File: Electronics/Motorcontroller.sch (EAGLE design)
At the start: 33 parts, among them Q1 IRFZ48V, Q2 IRF4905V, Q3 IRFZ48V, Q4 IRF4905V, Q5 IRFZ48V, Q6 IRF4905V, Q7 IRFZ48V, Q8 IRF4905V, X3 24V Batt

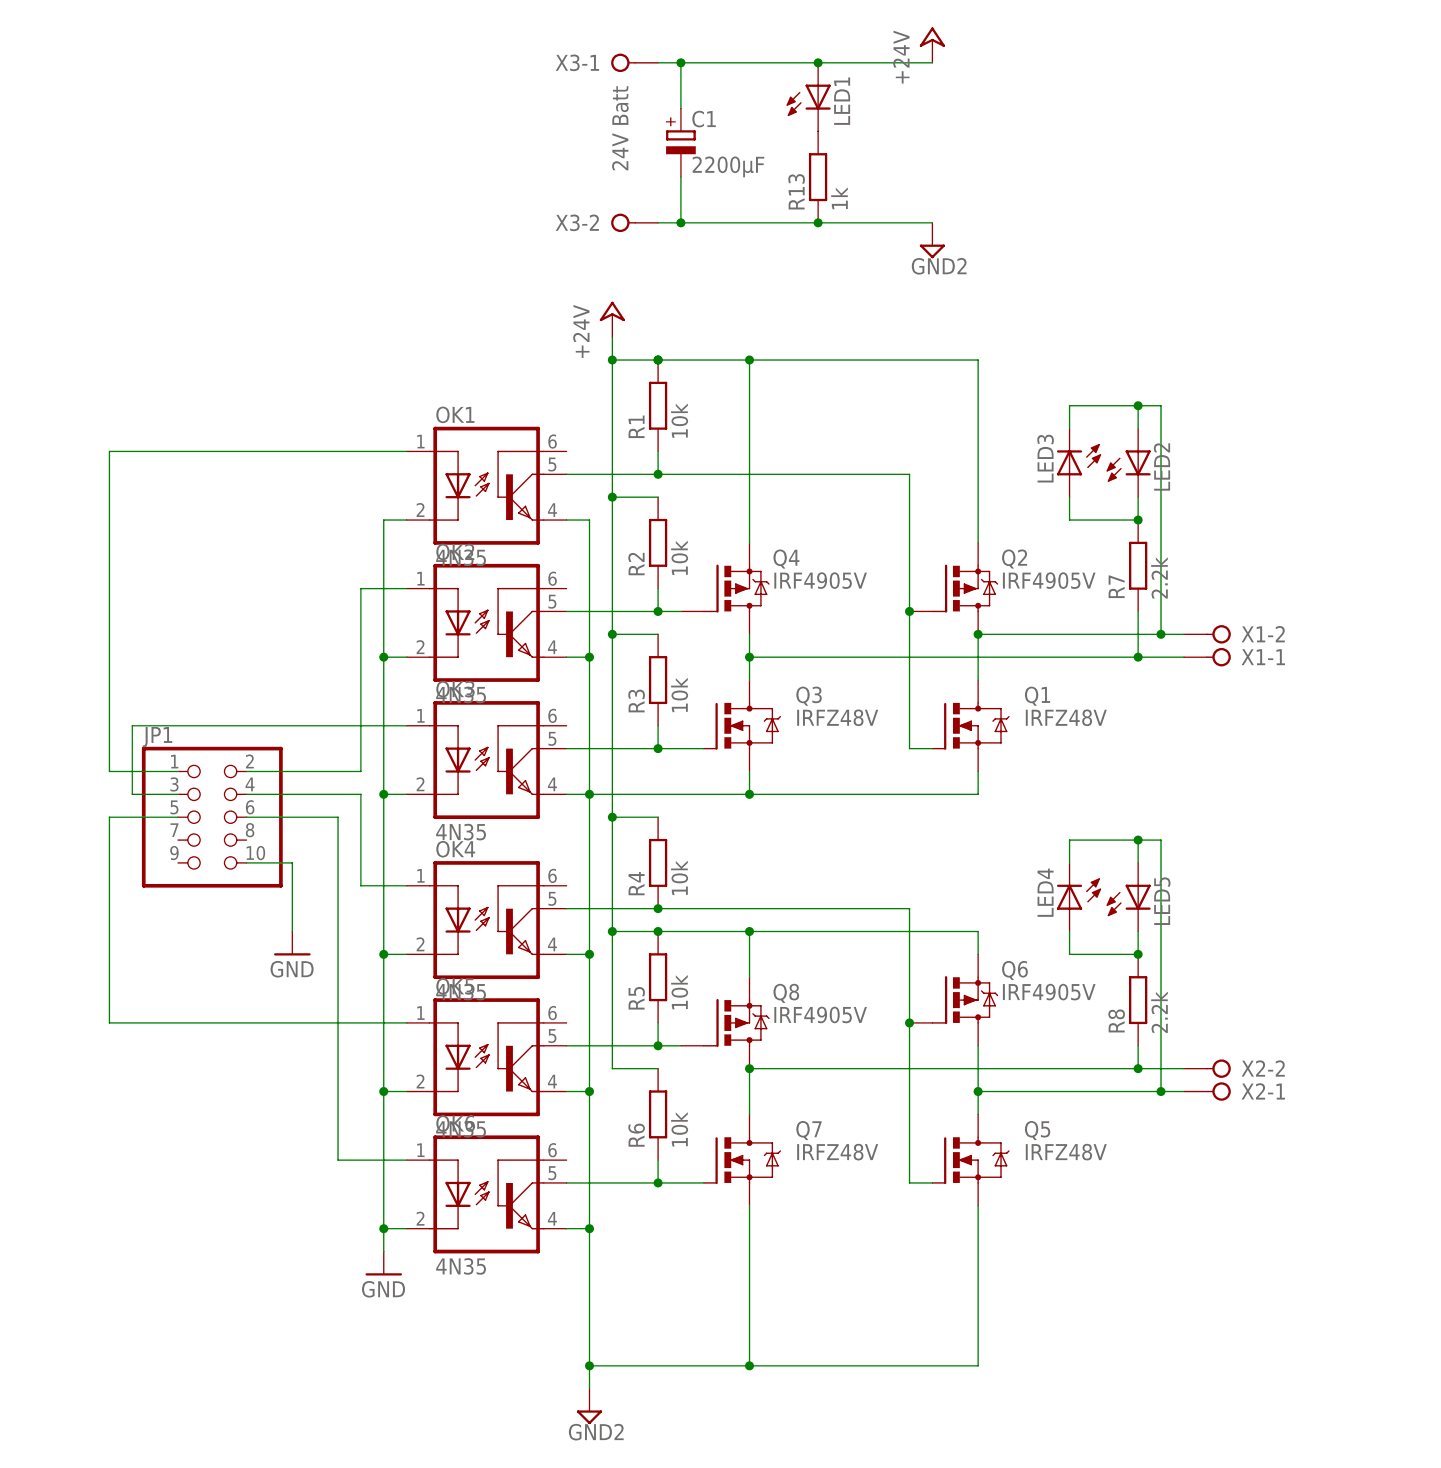
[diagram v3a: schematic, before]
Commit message: Redesign of motorboard. Closes #30
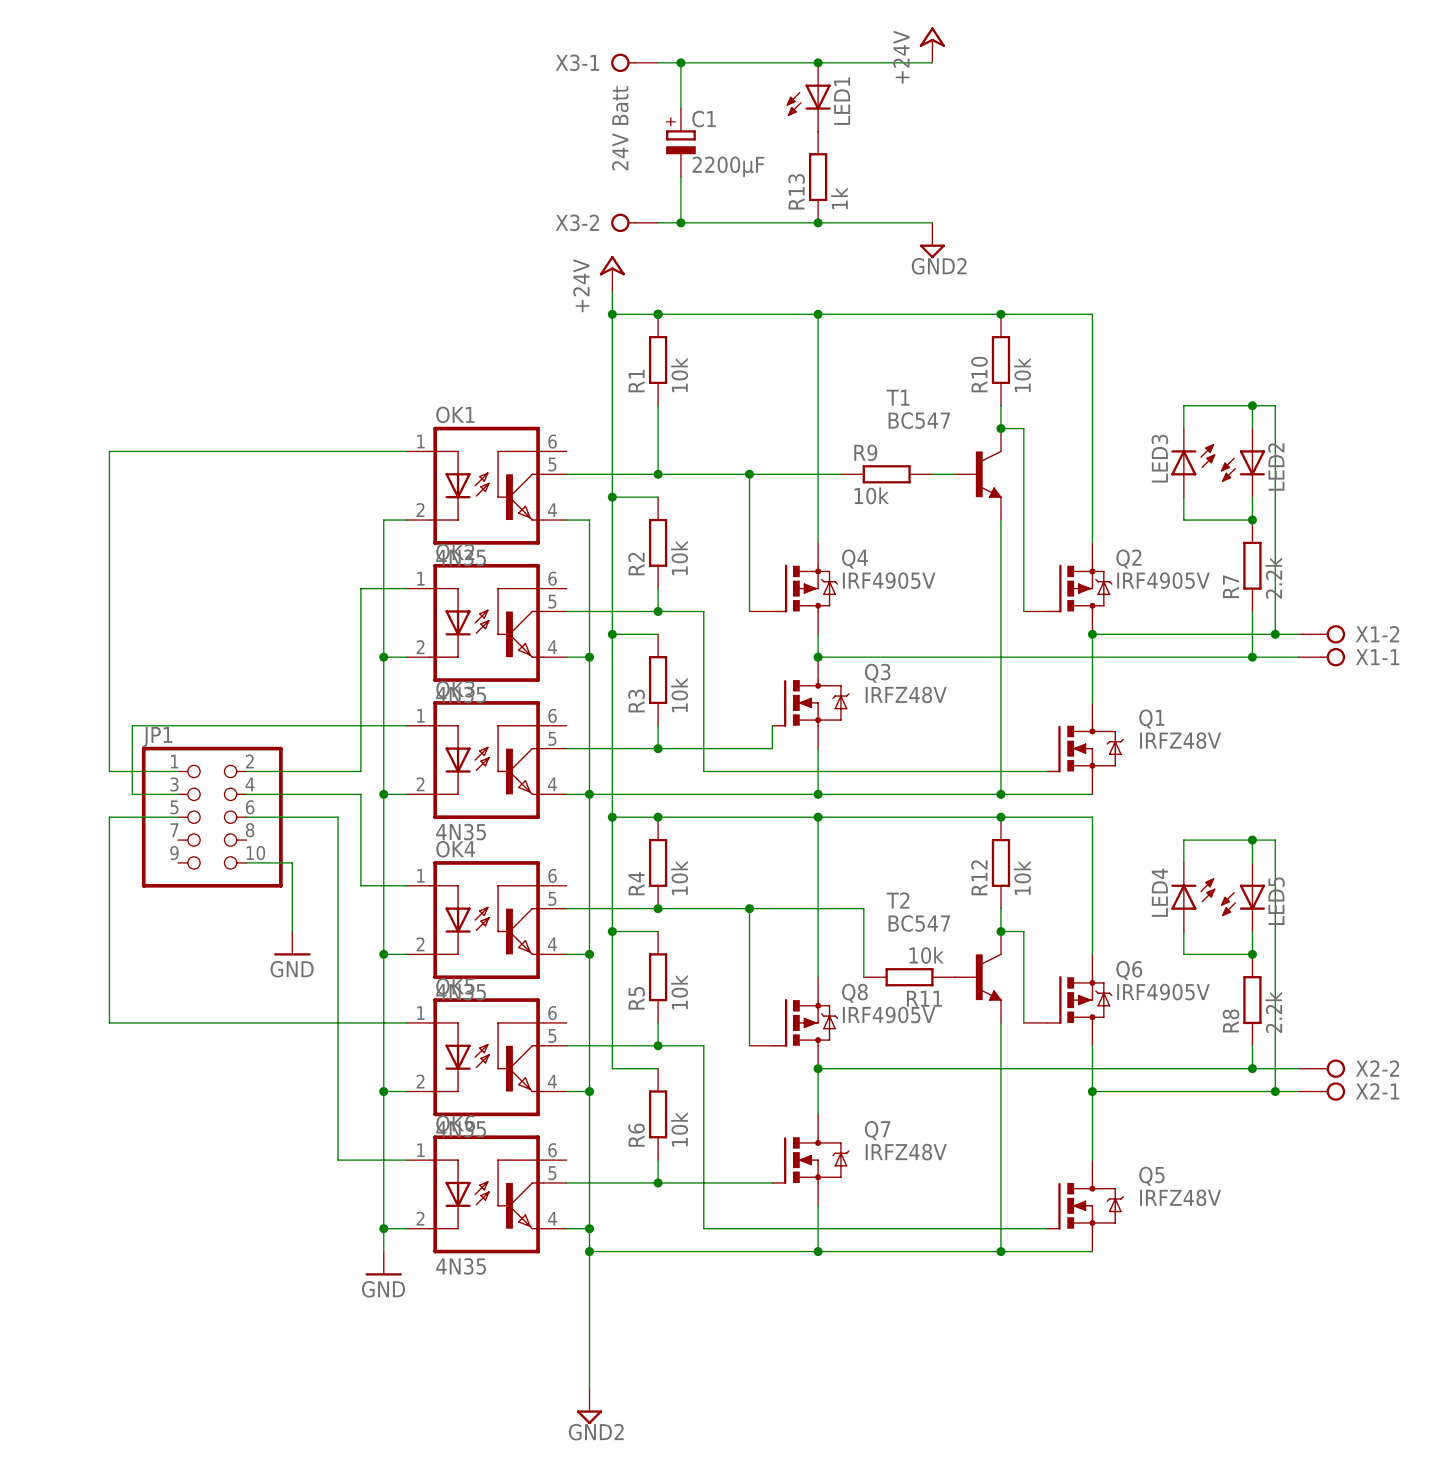
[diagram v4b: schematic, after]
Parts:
- added R10, R9: 10k, rcl:R-EU_0207/7
- added R11, R12: 10k, rcl:R-EU_0207/10
- added T1, T2: BC547, transistor:BC547
- R4: device rcl:R-EU_0207/10 -> rcl:R-EU_0207/7
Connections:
- new net N$14: R9.2, T1.B
- new net N$15: Q2.G, R10.1, T1.C
- new net N$16: OK4.COL, Q8.G, R11.2, R4.1
- new net N$18: R11.1, T2.B
- net +24V: now also R10.2, R12.2
- net GND2: now also T1.E, T2.E
- net N$12: now also Q4.G, R9.1; no longer Q1.G, Q2.G
- net N$19: now also R12.1, T2.C; no longer OK4.COL, Q5.G, R4.1
- net N$21: now also Q5.G; no longer Q8.G
- net N$9: now also Q1.G; no longer Q4.G
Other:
- moved on the sheet: LED2, LED3, LED4, LED5, Q1, Q2, Q3, Q4, Q5, Q6, Q7, Q8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

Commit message: New motorcontroller with pull-down
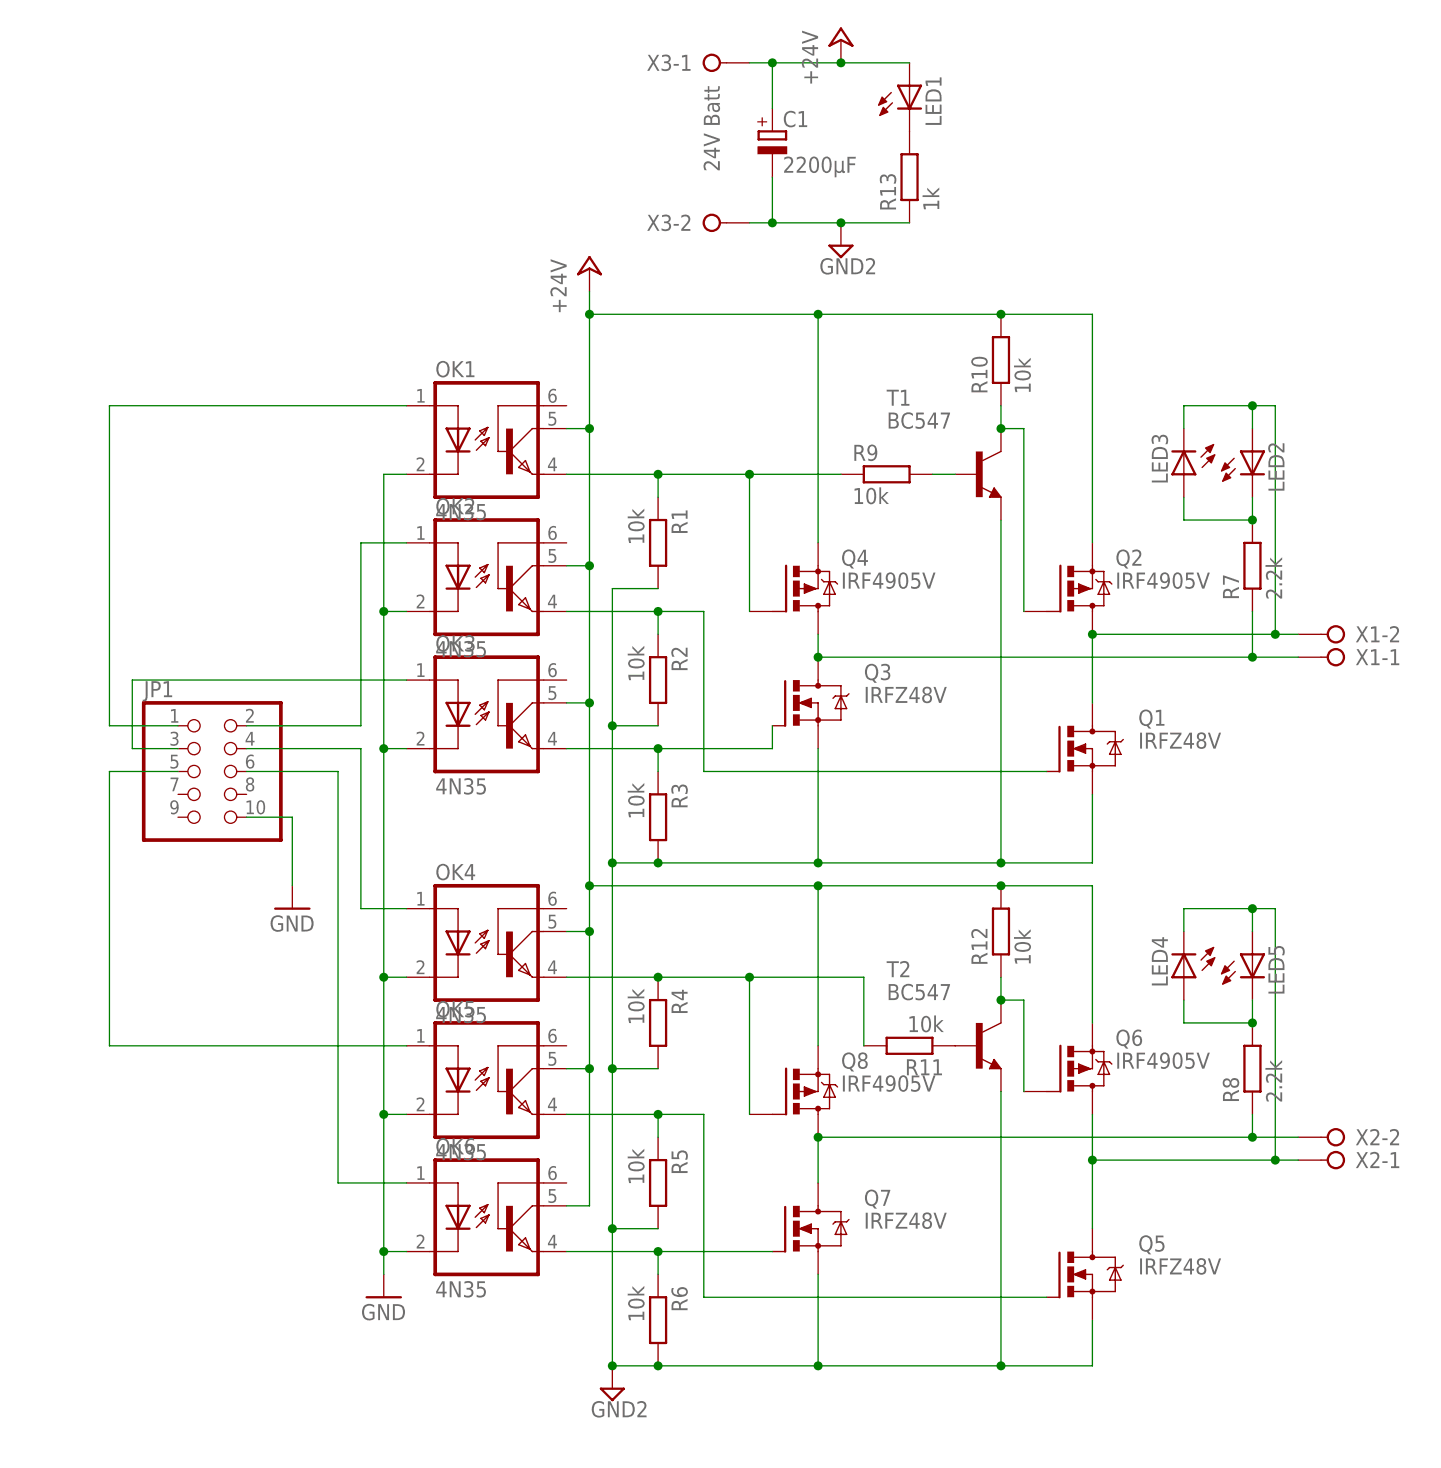
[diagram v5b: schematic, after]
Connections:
- net +24V: now also OK1.COL, OK2.COL, OK3.COL, OK4.COL, OK5.COL, OK6.COL; no longer R1.2, R2.2, R3.2, R4.2, R5.2, R6.2
- net GND2: now also R1.2, R2.2, R3.2, R4.2, R5.2, R6.2; no longer OK1.EMI, OK2.EMI, OK3.EMI, OK4.EMI, OK5.EMI, OK6.EMI
- net N$12: now also OK1.EMI; no longer OK1.COL
- net N$13: now also OK3.EMI; no longer OK3.COL
- net N$16: now also OK4.EMI; no longer OK4.COL
- net N$21: now also OK5.EMI; no longer OK5.COL
- net N$22: now also OK6.EMI; no longer OK6.COL
- net N$9: now also OK2.EMI; no longer OK2.COL
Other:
- moved on the sheet: C1, JP1, LED1, LED4, LED5, OK1, OK2, OK3, OK4, OK5, OK6, Q5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
